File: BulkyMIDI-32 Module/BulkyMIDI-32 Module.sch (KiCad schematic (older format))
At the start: 37 parts, among them IC1 OLED, J1 DC IN, J2 MIDI OUT, J3 MIDI IN, J4 Faceplate, J5 MIDI THRU, J6 Serial, J7 Conn_Extras, M1 Mounting, M2 Mounting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

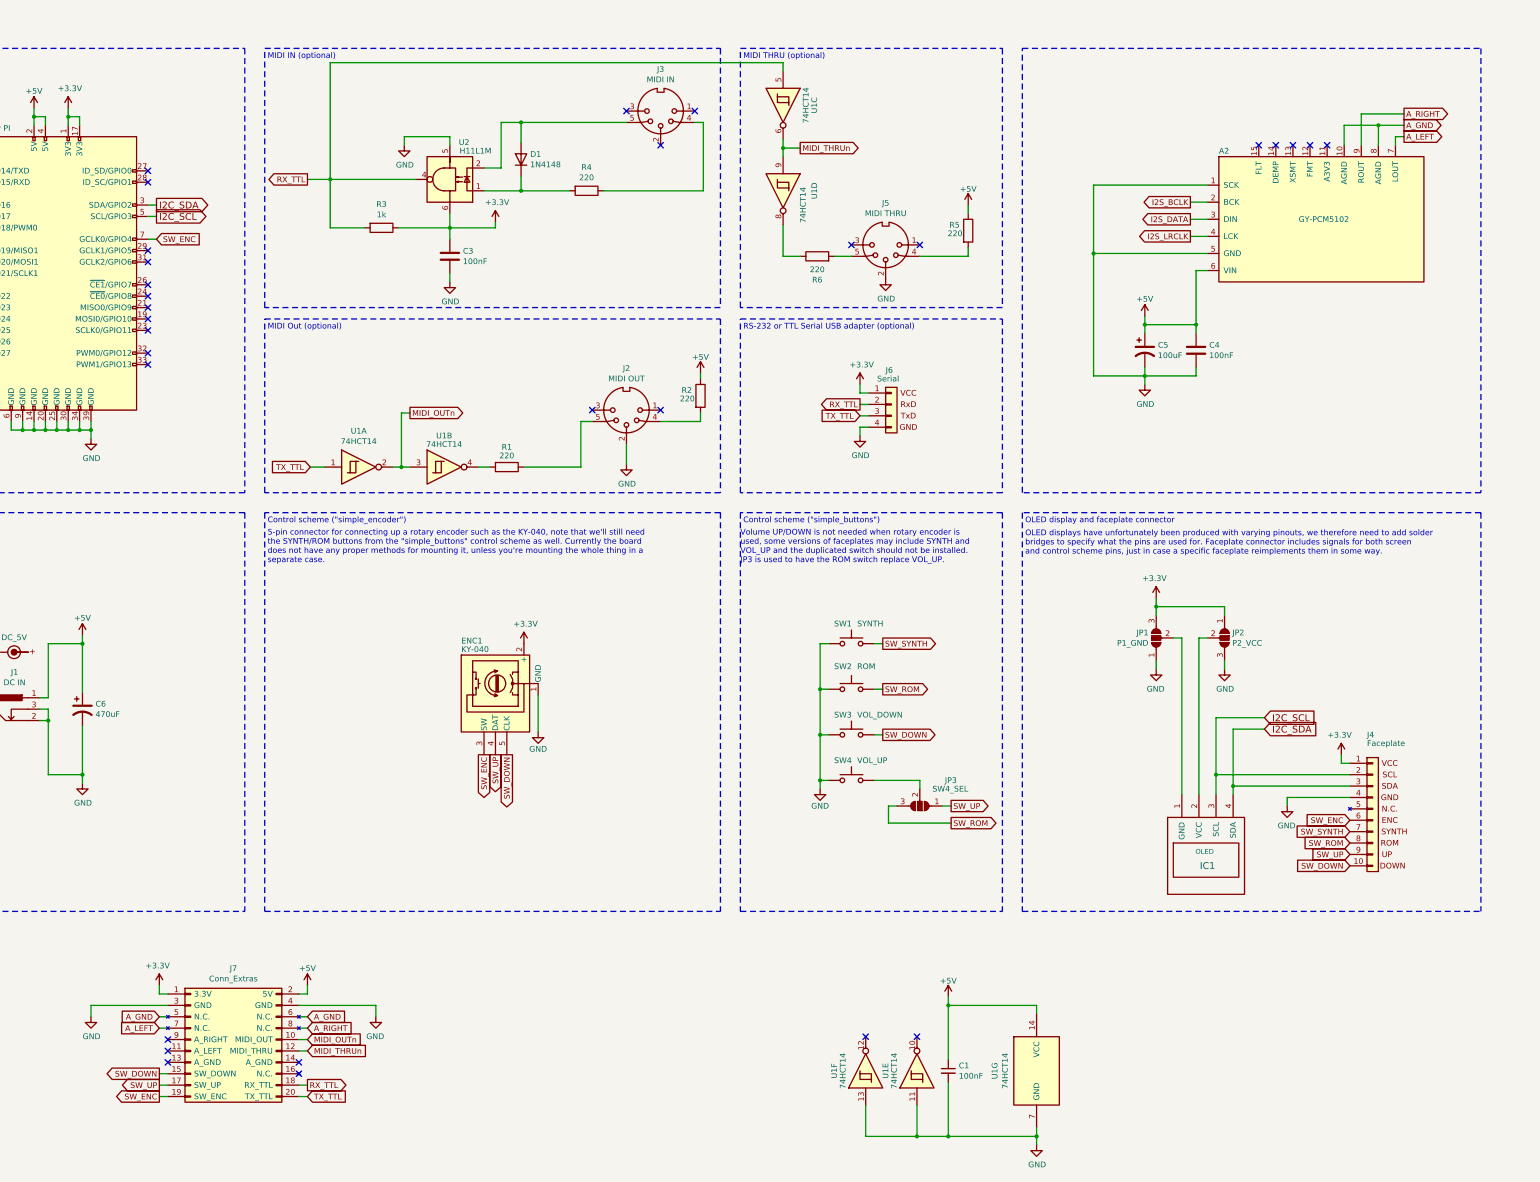
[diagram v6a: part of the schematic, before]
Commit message: Added jumpers to manually link audio to extras
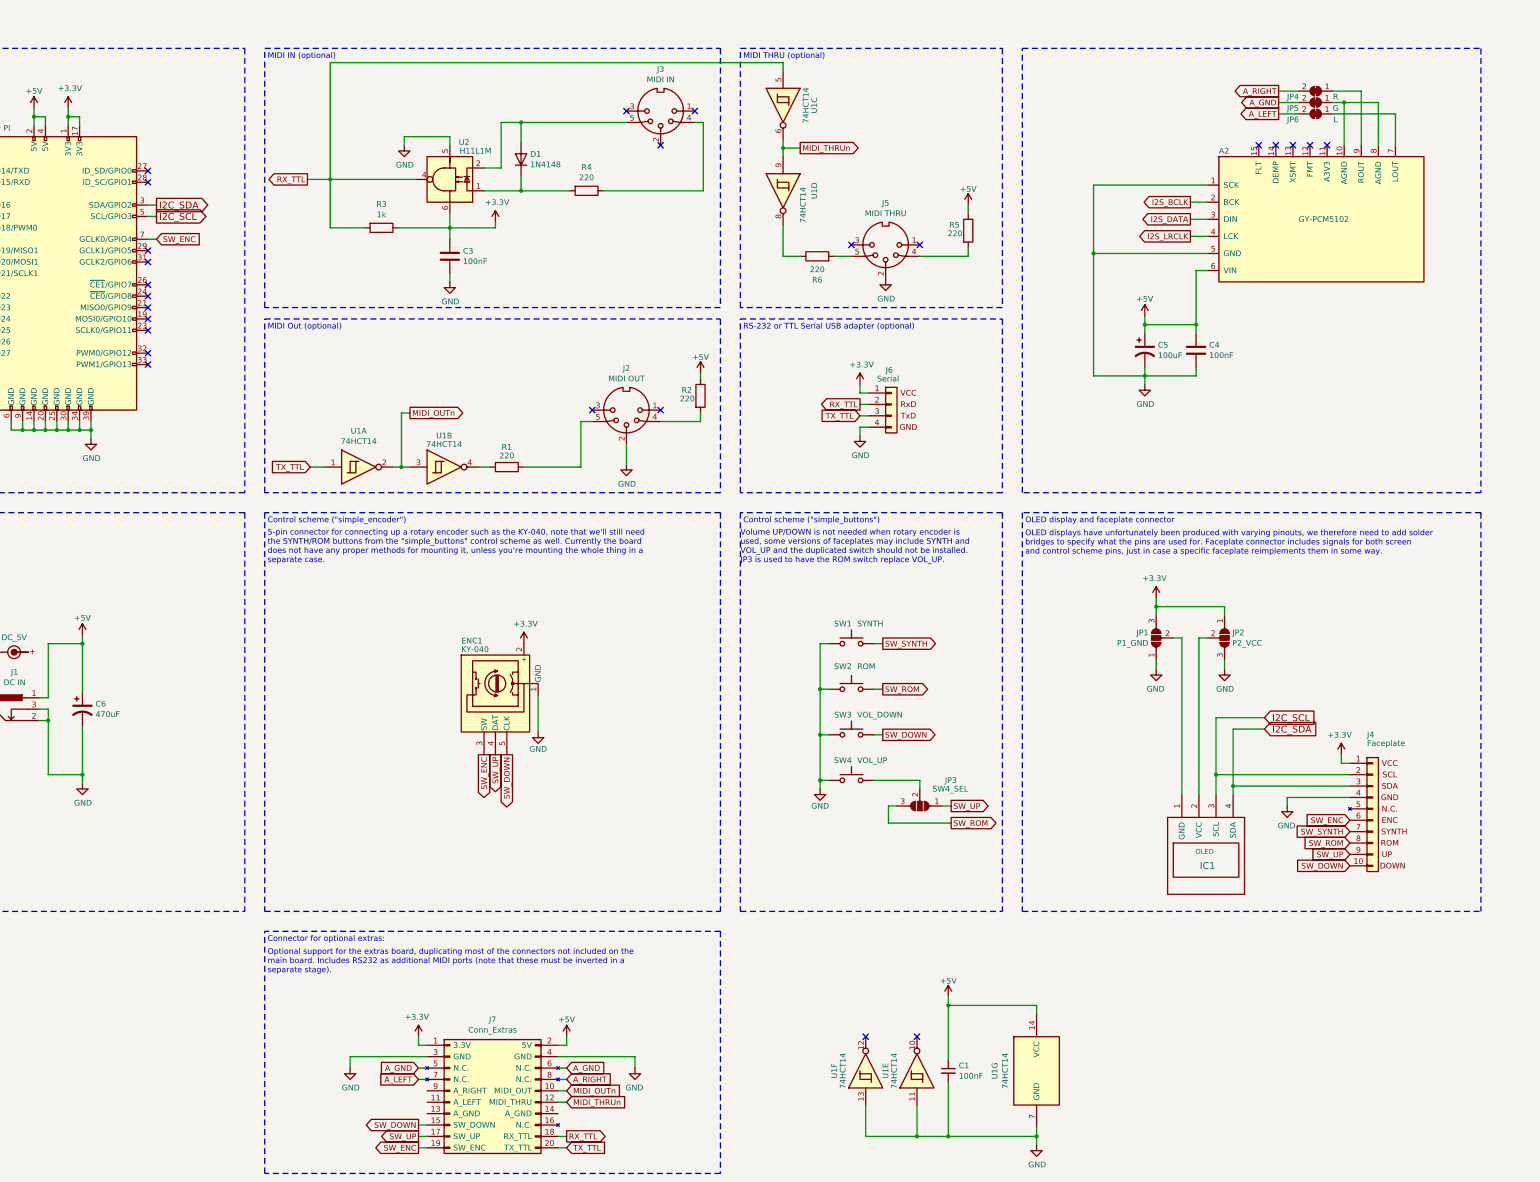
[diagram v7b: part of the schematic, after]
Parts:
- added JP4: R, Jumper:SolderJumper-2_P1.3mm_Open_TrianglePad1.0x1.5mm, symbol Jumper:SolderJumper_2_Bridged
- added JP5: G, Jumper:SolderJumper-2_P1.3mm_Open_TrianglePad1.0x1.5mm, symbol Jumper:SolderJumper_2_Bridged
- added JP6: L, Jumper:SolderJumper-2_P1.3mm_Open_TrianglePad1.0x1.5mm, symbol Jumper:SolderJumper_2_Bridged
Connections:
- net A_GND: now also JP5.2 (B); no longer A2.10 (AGND), A2.8 (AGND)
- net A_LEFT: now also JP6.2 (B); no longer A2.7 (LOUT)
- net A_RIGHT: now also JP4.2 (B); no longer A2.9 (ROUT)
- new net: A2.10 (AGND), A2.8 (AGND), JP5.1 (A)
- new net: A2.7 (LOUT), JP6.1 (A)
- new net: A2.9 (ROUT), JP4.1 (A)
- no-connect marks 36 -> 31
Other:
- note added: "Connector for optional extras:"
- note added: "Optional support for the extras board, duplicating most of the connectors not included on the\nmain board. Includes RS232 as additional MIDI ports (note that these must be inverted in a \nseparate stage)."
- moved on the sheet: J7
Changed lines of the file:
@@
 L BulkyMIDI:Conn_Extras J7
 U 1 1 62376277
-P 4375 9975
-F 0 "J7" H 4425 10600 50  0000 C CNN
-F 1 "Conn_Extras" H 4425 10509 50  0000 C CNN
-F 2 "Connector_PinSocket_2.54mm:PinSocket_2x10_P2.54mm_Vertical" H 4375 9975 50  0001 C CNN
-F 3 "~" H 4375 9975 50  0001 C CNN
-	1    4375 9975
+P 6650 10425
+F 0 "J7" H 6700 11050 50  0000 C CNN
+F 1 "Conn_Extras" H 6700 10959 50  0000 C CNN
+F 2 "Connector_PinSocket_2.54mm:PinSocket_2x10_P2.54mm_Vertical" H 6650 10425 50  0001 C CNN
+F 3 "~" H 6650 10425 50  0001 C CNN
+	1    6650 10425
 	1    0    0    -1
 $EndComp
-Text GLabel 14700 2050 2    50   Output ~ 0
+Text GLabel 13600 1850 0    50   Output ~ 0
 A_LEFT
-Wire Wire Line
-	14625 2125 14625 2050
-Wire Wire Line
-	14625 2050 14700 2050
-Text GLabel 14700 1950 2    50   Output ~ 0
+Text GLabel 13600 1750 0    50   Output ~ 0
 A_GND
-Wire Wire Line
-	14475 2125 14475 1950
-Wire Wire Line
-	14475 1950 14700 1950
-Wire Wire Line
-	14475 1950 14175 1950
-Wire Wire Line
-	14175 1950 14175 2125
-Connection ~ 14475 1950
-Text GLabel 14700 1850 2    50   Output ~ 0
+Text GLabel 13600 1650 0    50   Output ~ 0
 A_RIGHT
-Wire Wire Line
-	14700 1850 14325 1850
-Wire Wire Line
-	14325 1850 14325 2125
 $Comp
 L power:+5V #PWR0102
 U 1 1 623DF6A7
-P 5075 9500
-F 0 "#PWR0102" H 5075 9350 50  0001 C CNN
-F 1 "+5V" H 5075 9650 50  0000 C CNN
-F 2 "" H 5075 9500 50  0001 C CNN
-F 3 "" H 5075 9500 50  0001 C CNN
-	1    5075 9500
+P 7350 9950
+F 0 "#PWR0102" H 7350 9800 50  0001 C CNN
+F 1 "+5V" H 7350 10100 50  0000 C CNN
+F 2 "" H 7350 9950 50  0001 C CNN
+F 3 "" H 7350 9950 50  0001 C CNN
+	1    7350 9950
 	1    0    0    -1
 $EndComp
 Wire Wire Line
-	3775 9500 3775 9575
-Wire Wire Line
-	3775 9575 3850 9575
-Wire Wire Line
-	5075 9500 5075 9575
-Wire Wire Line
-	5000 9575 5075 9575
+	6050 9950 6050 10025
+Wire Wire Line
+	6050 10025 6125 10025
+Wire Wire Line
+	7350 9950 7350 10025
+Wire Wire Line
+	7275 10025 7350 10025
 $Comp
 L power:+3.3V #PWR0115
 U 1 1 6242ADA1
-P 3775 9500
-F 0 "#PWR0115" H 3775 9350 50  0001 C CNN
-F 1 "+3.3V" H 3790 9673 50  0000 C CNN
-F 2 "" H 3775 9500 50  0001 C CNN
-F 3 "" H 3775 9500 50  0001 C CNN
-	1    3775 9500
+P 6050 9950
+F 0 "#PWR0115" H 6050 9800 50  0001 C CNN
+F 1 "+3.3V" H 6065 10123 50  0000 C CNN
+F 2 "" H 6050 9950 50  0001 C CNN
+F 3 "" H 6050 9950 50  0001 C CNN
+	1    6050 9950
 	-1   0    0    -1
 $EndComp
-Text GLabel 3775 9875 0    50   Input ~ 0
+Text GLabel 6050 10325 0    50   Input ~ 0
 A_LEFT
-Text GLabel 5075 9775 2    50   Input ~ 0
+Text GLabel 7350 10225 2    50   Input ~ 0
 A_GND
-Text GLabel 5075 9875 2    50   Input ~ 0
+Text GLabel 7350 10325 2    50   Input ~ 0
 A_RIGHT
 Wire Wire Line
-	5075 9875 5000 9875
-Text GLabel 3775 9775 0    50   Input ~ 0
+	7350 10325 7275 10325
+Text GLabel 6050 10225 0    50   Input ~ 0
 A_GND
 Wire Wire Line
-	3775 9775 3850 9775
-Wire Wire Line
-	3775 9875 3850 9875
-Wire Wire Line
-	3850 9675 3175 9675
-Wire Wire Line
-	3175 9675 3175 9775
+	6050 10225 6125 10225
+Wire Wire Line
+	6050 10325 6125 10325
+Wire Wire Line
+	6125 10125 5450 10125
+Wire Wire Line
+	5450 10125 5450 10225
 $Comp
 L power:GND #PWR0116
 U 1 1 62487A35
-P 3175 9775
-F 0 "#PWR0116" H 3175 9525 50  0001 C CNN
-F 1 "GND" H 3180 9602 50  0000 C CNN
-F 2 "" H 3175 9775 50  0001 C CNN
-F 3 "" H 3175 9775 50  0001 C CNN
-	1    3175 9775
+P 5450 10225
+F 0 "#PWR0116" H 5450 9975 50  0001 C CNN
+F 1 "GND" H 5455 10052 50  0000 C CNN
+F 2 "" H 5450 10225 50  0001 C CNN
+F 3 "" H 5450 10225 50  0001 C CNN
+	1    5450 10225
 	1    0    0    -1
 $EndComp
 Wire Wire Line
-	5000 9675 5675 9675
-Wire Wire Line
-	5675 9675 5675 9775
+	7275 10125 7950 10125
+Wire Wire Line
+	7950 10125 7950 10225
 $Comp
 L power:GND #PWR0117
 U 1 1 62492E5B
-P 5675 9775
-F 0 "#PWR0117" H 5675 9525 50  0001 C CNN
-F 1 "GND" H 5680 9602 50  0000 C CNN
-F 2 "" H 5675 9775 50  0001 C CNN
-F 3 "" H 5675 9775 50  0001 C CNN
-	1    5675 9775
+P 7950 10225
+F 0 "#PWR0117" H 7950 9975 50  0001 C CNN
+F 1 "GND" H 7955 10052 50  0000 C CNN
+F 2 "" H 7950 10225 50  0001 C CNN
+F 3 "" H 7950 10225 50  0001 C CNN
+	1    7950 10225
 	-1   0    0    -1
 $EndComp
 Wire Wire Line
-	5075 9775 5000 9775
-NoConn ~ 3850 9975
-NoConn ~ 3850 10075
-NoConn ~ 3850 10175
-Wire Wire Line
-	5000 10075 5075 10075
-Wire Wire Line
-	5075 9975 5000 9975
+	7350 10225 7275 10225
+Wire Wire Line
+	7275 10525 7350 10525
+Wire Wire Line
+	7350 10425 7275 10425
 Text GLabel 9400 2150 2    50   Output ~ 0
 MIDI_THRUn
@@
 Wire Wire Line
 	5275 1400 9250 1400
-NoConn ~ 5000 10175
-NoConn ~ 5000 10275
-Text GLabel 5075 10375 2    50   Output ~ 0
+Text GLabel 7350 10825 2    50   Output ~ 0
 RX_TTL
 Wire Wire Line
-	5075 10475 5000 10475
-Text GLabel 5075 10475 2    50   Input ~ 0
+	7350 10925 7275 10925
+Text GLabel 7350 10925 2    50   Input ~ 0
 TX_TTL
 Wire Wire Line
-	5075 10375 5000 10375
-Text GLabel 3775 10475 0    50   Output ~ 0
+	7350 10825 7275 10825
+Text GLabel 6050 10925 0    50   Output ~ 0
 SW_ENC
-Text GLabel 3775 10375 0    50   Output ~ 0
+Text GLabel 6050 10825 0    50   Output ~ 0
 SW_UP
-Text GLabel 3775 10275 0    50   Output ~ 0
+Text GLabel 6050 10725 0    50   Output ~ 0
 SW_DOWN
 Wire Wire Line
-	3775 10275 3850 10275
-Wire Wire Line
-	3850 10375 3775 10375
-Wire Wire Line
-	3775 10475 3850 10475
+	6050 10725 6125 10725
+Wire Wire Line
+	6125 10825 6050 10825
+Wire Wire Line
+	6050 10925 6125 10925
 Text GLabel 5975 4475 2    50   Output ~ 0
 MIDI_OUTn
-Text GLabel 5075 9975 2    50   Input ~ 0
+Text GLabel 7350 10425 2    50   Input ~ 0
 MIDI_OUTn
 NoConn ~ 9975 9950
@@
 Wire Wire Line
 	9250 2150 9250 2225
-Text GLabel 5075 10075 2    50   Input ~ 0
+Text GLabel 7350 10525 2    50   Input ~ 0
 MIDI_THRUn
+Wire Notes Line
+	8700 9025 4700 9025
+Text Notes 4725 9125 0    50   ~ 0
+Connector for optional extras:
+Wire Notes Line
+	8700 9025 8700 11150
+Wire Notes Line
+	8700 11150 4700 11150
+Wire Notes Line
+	4700 11150 4700 9025
+Text Notes 4725 9400 0    50   ~ 0
+Optional support for the extras board, duplicating most of the connectors not included on the\nmain board. Includes RS232 as additional MIDI ports (note that these must be inverted in a \nseparate stage).
+$Comp
+L Jumper:SolderJumper_2_Bridged JP4
+U 1 1 62D4CD43
+P 13925 1650
+F 0 "JP4" H 14125 1700 50  0000 C CNN
+F 1 "R" H 13750 1700 50  0000 C CNN
+F 2 "Jumper:SolderJumper-2_P1.3mm_Open_TrianglePad1.0x1.5mm" H 13925 1650 50  0001 C CNN
+F 3 "~" H 13925 1650 50  0001 C CNN
+	1    13925 1650
+	-1   0    0    1
+$EndComp
+$Comp
+L Jumper:SolderJumper_2_Bridged JP5
+U 1 1 62D70E02
+P 13925 1750
+F 0 "JP5" H 14125 1800 50  0000 C CNN
+F 1 "G" H 13750 1800 50  0000 C CNN
+F 2 "Jumper:SolderJumper-2_P1.3mm_Open_TrianglePad1.0x1.5mm" H 13925 1750 50  0001 C CNN
+F 3 "~" H 13925 1750 50  0001 C CNN
+	1    13925 1750
+	-1   0    0    1
+$EndComp
+$Comp
+L Jumper:SolderJumper_2_Bridged JP6
+U 1 1 62D7C338
+P 13925 1850
+F 0 "JP6" H 14125 1900 50  0000 C CNN
+F 1 "L" H 13750 1900 50  0000 C CNN
+F 2 "Jumper:SolderJumper-2_P1.3mm_Open_TrianglePad1.0x1.5mm" H 13925 1850 50  0001 C CNN
+F 3 "~" H 13925 1850 50  0001 C CNN
+	1    13925 1850
+	-1   0    0    1
+$EndComp
+Wire Wire Line
+	13600 1650 13775 1650
+Wire Wire Line
+	13600 1750 13775 1750
+Wire Wire Line
+	13600 1850 13775 1850
+Wire Wire Line
+	14175 1750 14075 1750
+Wire Wire Line
+	14175 1750 14475 1750
+Connection ~ 14175 1750
+Wire Wire Line
+	14175 1750 14175 2125
+Wire Wire Line
+	14475 1750 14475 2125
+Wire Wire Line
+	14325 1650 14075 1650
+Wire Wire Line
+	14325 1650 14325 2125
+Wire Wire Line
+	14625 1850 14075 1850
+Wire Wire Line
+	14625 1850 14625 2125
 $EndSCHEMATC

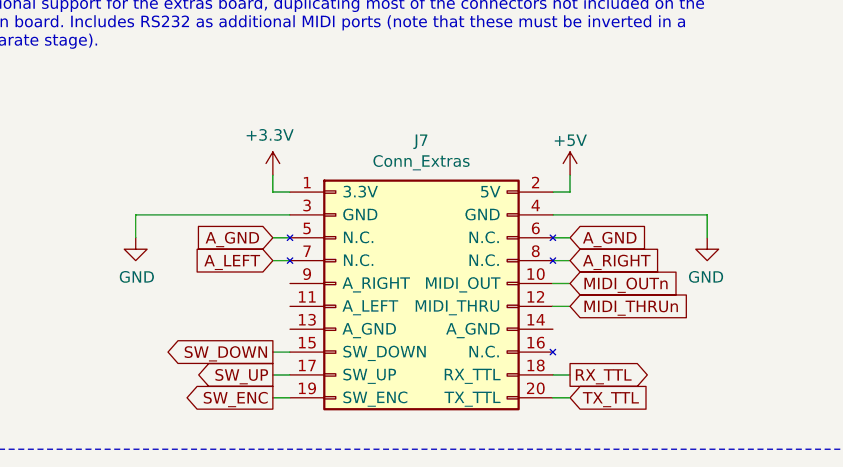
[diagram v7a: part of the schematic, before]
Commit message: Routed tracks for extras board
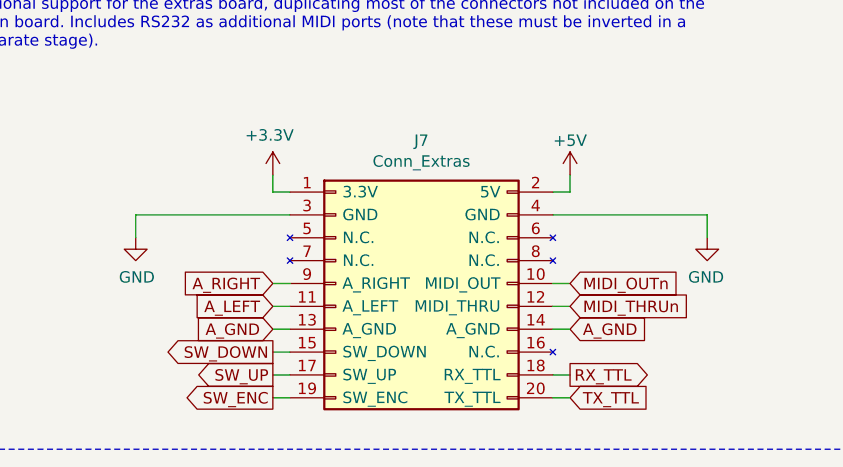
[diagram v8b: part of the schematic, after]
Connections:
- net A_GND: now also J7.13 (A_GND), J7.14 (A_GND); no longer J7.5 (N.C.), J7.6 (N.C.)
- net A_LEFT: now also J7.11 (A_LEFT); no longer J7.7 (N.C.)
- net A_RIGHT: now also J7.9 (A_RIGHT); no longer J7.8 (N.C.)
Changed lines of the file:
@@
 	-1   0    0    -1
 $EndComp
-Text GLabel 6050 10325 0    50   Input ~ 0
+Text GLabel 6050 10525 0    50   Input ~ 0
 A_LEFT
-Text GLabel 7350 10225 2    50   Input ~ 0
+Text GLabel 7350 10625 2    50   Input ~ 0
 A_GND
-Text GLabel 7350 10325 2    50   Input ~ 0
+Text GLabel 6050 10425 0    50   Input ~ 0
 A_RIGHT
 Wire Wire Line
-	7350 10325 7275 10325
-Text GLabel 6050 10225 0    50   Input ~ 0
+	6050 10425 6125 10425
+Text GLabel 6050 10625 0    50   Input ~ 0
 A_GND
 Wire Wire Line
-	6050 10225 6125 10225
+	6050 10625 6125 10625
 Wire Wire Line
-	6050 10325 6125 10325
+	6050 10525 6125 10525
 Wire Wire Line
 	6125 10125 5450 10125
@@
 $EndComp
 Wire Wire Line
-	7350 10225 7275 10225
+	7350 10625 7275 10625
 Wire Wire Line
 	7275 10525 7350 10525
